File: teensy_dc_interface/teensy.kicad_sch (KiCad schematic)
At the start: 1 part, among them U2 Teensy4.0

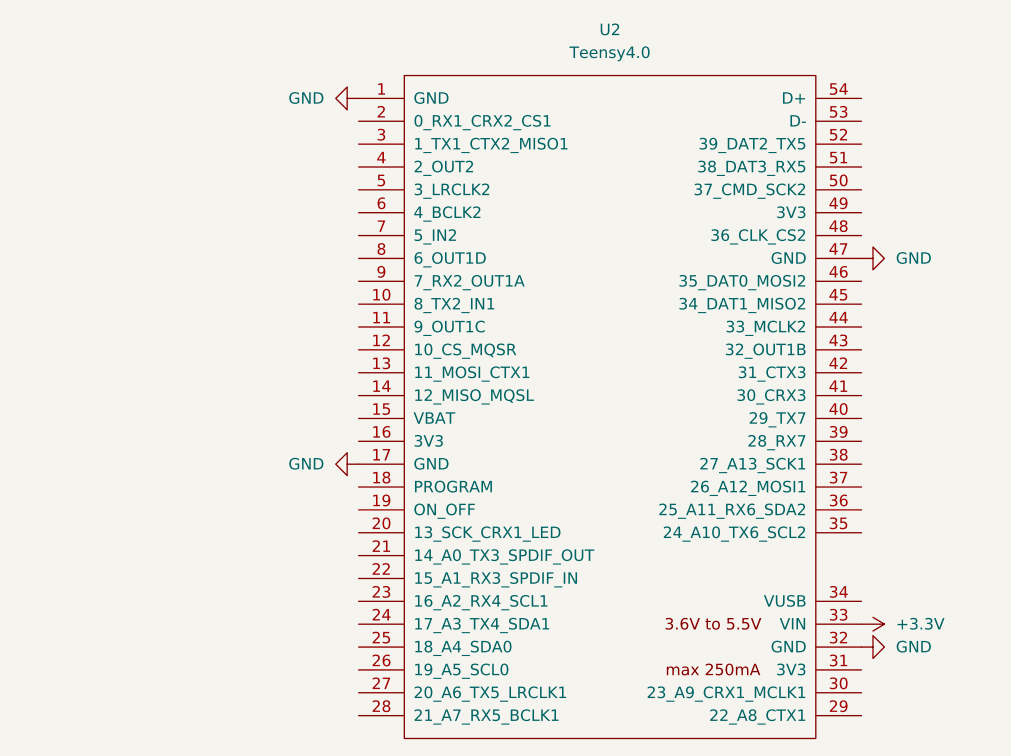
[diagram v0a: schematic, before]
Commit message: teensy to dac connections
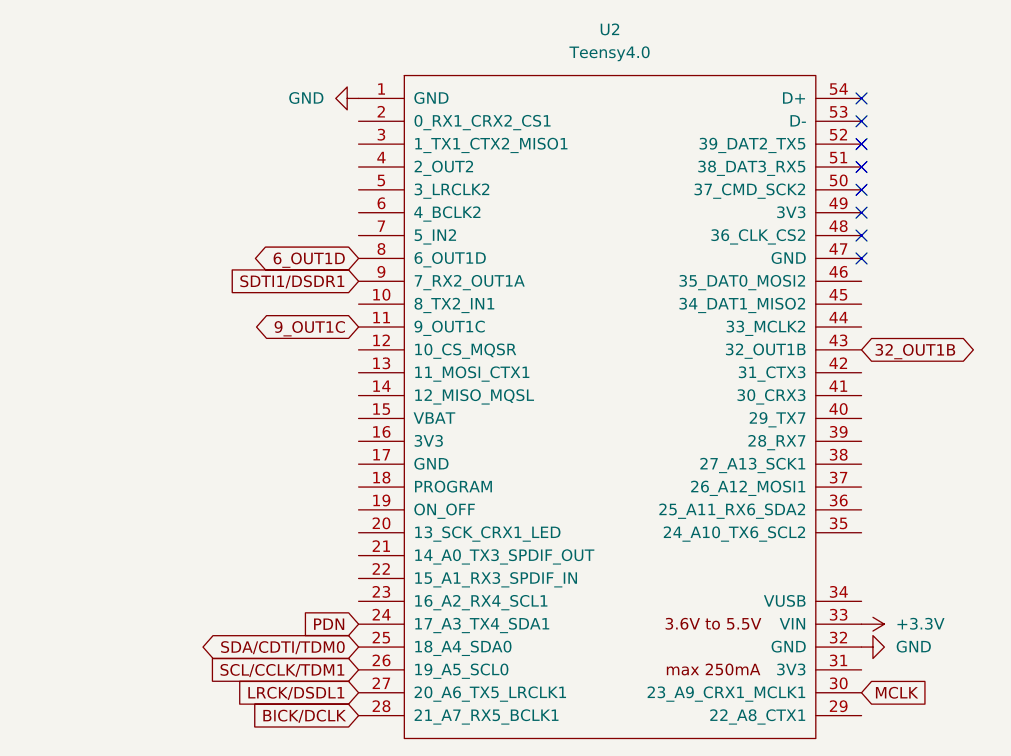
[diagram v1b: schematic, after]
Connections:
- net GND: no longer U2.17 (GND), U2.47 (GND)
- net 9_OUT1C: now reaches U2.11 (9_OUT1C)
- net PDN: now reaches U2.24 (17_A3_TX4_SDA1)
- net SDA/CDTI/TDM0: now reaches U2.25 (18_A4_SDA0)
- net SCL/CCLK/TDM1: now reaches U2.26 (19_A5_SCL0)
- net LRCK/DSDL1: now reaches U2.27 (20_A6_TX5_LRCLK1)
- net BICK/DCLK: now reaches U2.28 (21_A7_RX5_BCLK1)
- net MCLK: now reaches U2.30 (23_A9_CRX1_MCLK1)
- net 32_OUT1B: now reaches U2.43 (32_OUT1B)
- net 6_OUT1D: now reaches U2.8 (6_OUT1D)
- net SDTI1/DSDR1: now reaches U2.9 (7_RX2_OUT1A)
- no-connect marks 0 -> 8
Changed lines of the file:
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@@
 	(generator_version "8.0")
 	(paper "A4")
+	(no_connect
+		(at 110.49 53.34)
+	)
+	(no_connect
+		(at 110.49 58.42)
+	)
+	(no_connect
+		(at 110.49 50.8)
+	)
+	(no_connect
+		(at 110.49 66.04)
+	)
+	(no_connect
+		(at 110.49 55.88)
+	)
+	(no_connect
+		(at 110.49 60.96)
+	)
+	(no_connect
+		(at 110.49 68.58)
+	)
+	(no_connect
+		(at 110.49 63.5)
+	)
+	(global_label "6_OUT1D"
+		(shape bidirectional)
+		(at 54.61 68.58 180)
+		(effects
+			(font
+				(size 1.27 1.27)
+			)
+			(justify right)
+		)
+		(property "Intersheetrefs" "${INTERSHEET_REFS}"
+			(at 54.61 68.58 0)
+			(effects
+				(font
+					(size 1.27 1.27)
+				)
+				(hide yes)
+			)
+		)
+	)
+	(global_label "SDTI1/DSDR1"
+		(shape input)
+		(at 54.61 71.12 180)
+		(effects
+			(font
+				(size 1.27 1.27)
+			)
+			(justify right)
+		)
+		(property "Intersheetrefs" "${INTERSHEET_REFS}"
+			(at 54.61 71.12 0)
+			(effects
+				(font
+					(size 1.27 1.27)
+				)
+				(hide yes)
+			)
+		)
+	)
+	(global_label "SDA/CDTI/TDM0"
+		(shape bidirectional)
+		(at 54.61 111.76 180)
+		(effects
+			(font
+				(size 1.27 1.27)
+			)
+			(justify right)
+		)
+		(property "Intersheetrefs" "${INTERSHEET_REFS}"
+			(at 54.61 111.76 0)
+			(effects
+				(font
+					(size 1.27 1.27)
+				)
+				(hide yes)
+			)
+		)
+	)
+	(global_label "32_OUT1B"
+		(shape bidirectional)
+		(at 110.49 78.74 0)
+		(effects
+			(font
+				(size 1.27 1.27)
+			)
+			(justify left)
+		)
+		(property "Intersheetrefs" "${INTERSHEET_REFS}"
+			(at 110.49 78.74 0)
+			(effects
+				(font
+					(size 1.27 1.27)
+				)
+				(hide yes)
+			)
+		)
+	)
+	(global_label "MCLK"
+		(shape input)
+		(at 110.49 116.84 0)
+		(effects
+			(font
+				(size 1.27 1.27)
+			)
+			(justify left)
+		)
+		(property "Intersheetrefs" "${INTERSHEET_REFS}"
+			(at 110.49 116.84 0)
+			(effects
+				(font
+					(size 1.27 1.27)
+				)
+				(hide yes)
+			)
+		)
+	)
+	(global_label "9_OUT1C"
+		(shape bidirectional)
+		(at 54.61 76.2 180)
+		(effects
+			(font
+				(size 1.27 1.27)
+			)
+			(justify right)
+		)
+		(property "Intersheetrefs" "${INTERSHEET_REFS}"
+			(at 54.61 76.2 0)
+			(effects
+				(font
+					(size 1.27 1.27)
+				)
+				(hide yes)
+			)
+		)
+	)
+	(global_label "BICK/DCLK"
+		(shape input)
+		(at 54.61 119.38 180)
+		(effects
+			(font
+				(size 1.27 1.27)
+			)
+			(justify right)
+		)
+		(property "Intersheetrefs" "${INTERSHEET_REFS}"
+			(at 54.61 119.38 0)
+			(effects
+				(font
+					(size 1.27 1.27)
+				)
+				(hide yes)
+			)
+		)
+	)
+	(global_label "SCL/CCLK/TDM1"
+		(shape input)
+		(at 54.61 114.3 180)
+		(effects
+			(font
+				(size 1.27 1.27)
+			)
+			(justify right)
+		)
+		(property "Intersheetrefs" "${INTERSHEET_REFS}"
+			(at 54.61 114.3 0)
+			(effects
+				(font
+					(size 1.27 1.27)
+				)
+				(hide yes)
+			)
+		)
+	)
+	(global_label "LRCK/DSDL1"
+		(shape input)
+		(at 54.61 116.84 180)
+		(effects
+			(font
+				(size 1.27 1.27)
+			)
+			(justify right)
+		)
+		(property "Intersheetrefs" "${INTERSHEET_REFS}"
+			(at 54.61 116.84 0)
+			(effects
+				(font
+					(size 1.27 1.27)
+				)
+				(hide yes)
+			)
+		)
+	)
+	(global_label "PDN"
+		(shape input)
+		(at 54.61 109.22 180)
+		(effects
+			(font
+				(size 1.27 1.27)
+			)
+			(justify right)
+		)
+		(property "Intersheetrefs" "${INTERSHEET_REFS}"
+			(at 54.61 109.22 0)
+			(effects
+				(font
+					(size 1.27 1.27)
+				)
+				(hide yes)
+			)
+		)
+	)
 	(symbol
 		(lib_id "4ms_Power-symbol:+3.3V")
@@
 					(unit 1)
 				)
-			)
-		)
-	)
-	(symbol
-		(lib_id "4ms_Power-symbol:GND")
-		(at 110.49 68.58 90)
-		(unit 1)
-		(exclude_from_sim no)
-		(in_bom yes)
-		(on_board yes)
-		(dnp no)
-		(fields_autoplaced yes)
-		(property "Reference" "#PWR038"
-			(at 116.84 68.58 0)
-			(effects
-				(font
-					(size 1.27 1.27)
-				)
-				(hide yes)
-			)
-		)
-		(property "Value" "GND"
-			(at 114.3 68.5799 90)
-			(effects
-				(font
-					(size 1.27 1.27)
-				)
-				(justify right)
-			)
-		)
-		(property "Footprint" ""
-			(at 110.49 68.58 0)
-			(effects
-				(font
-					(size 1.27 1.27)
-				)
-				(hide yes)
-			)
-		)
-		(property "Datasheet" ""
-			(at 110.49 68.58 0)
-			(effects
-				(font
-					(size 1.27 1.27)
-				)
-				(hide yes)
-			)
-		)
-		(property "Description" ""
-			(at 110.49 68.58 0)
-			(effects
-				(font
-					(size 1.27 1.27)
-				)
-				(hide yes)
-			)
-		)
-		(pin "1"
-		)
-		(instances
-			(project "teensy_dc_interface"
-				(path "/a4119639-42c9-4d05-afde-5b738907ed5a/cc1bffa6-65b3-47b9-9487-c9fe2212650d"
-					(reference "#PWR038")
-					(unit 1)
-				)
-			)
-		)
-	)
-	(symbol
-		(lib_id "4ms_Power-symbol:GND")
-		(at 54.61 91.44 270)
-		(unit 1)
-		(exclude_from_sim no)
-		(in_bom yes)
-		(on_board yes)
-		(dnp no)
-		(property "Reference" "#PWR037"
-			(at 48.26 91.44 0)
-			(effects
-				(font
-					(size 1.27 1.27)
-				)
-				(hide yes)
-			)
-		)
-		(property "Value" "GND"
-			(at 50.8 91.4399 90)
-			(effects
-				(font
-					(size 1.27 1.27)
-				)
-				(justify right)
-			)
-		)
-		(property "Footprint" ""
-			(at 54.61 91.44 0)
-			(effects
-				(font
-					(size 1.27 1.27)
-				)
-				(hide yes)
-			)
-		)
-		(property "Datasheet" ""
-			(at 54.61 91.44 0)
-			(effects
-				(font
-					(size 1.27 1.27)
-				)
-				(hide yes)
-			)
-		)
-		(property "Description" ""
-			(at 54.61 91.44 0)
-			(effects
-				(font
-					(size 1.27 1.27)
-				)
-				(hide yes)
-			)
-		)
-		(pin "1"
-		)
-		(instances
-			(project "teensy_dc_interface"
-				(path "/a4119639-42c9-4d05-afde-5b738907ed5a/cc1bffa6-65b3-47b9-9487-c9fe2212650d"
-					(reference "#PWR037")
-					(unit 1)
-				)

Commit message: Updated filtering between VREF's. Added separate power supply for Teensy on 5V. Added test points. Added ADC input
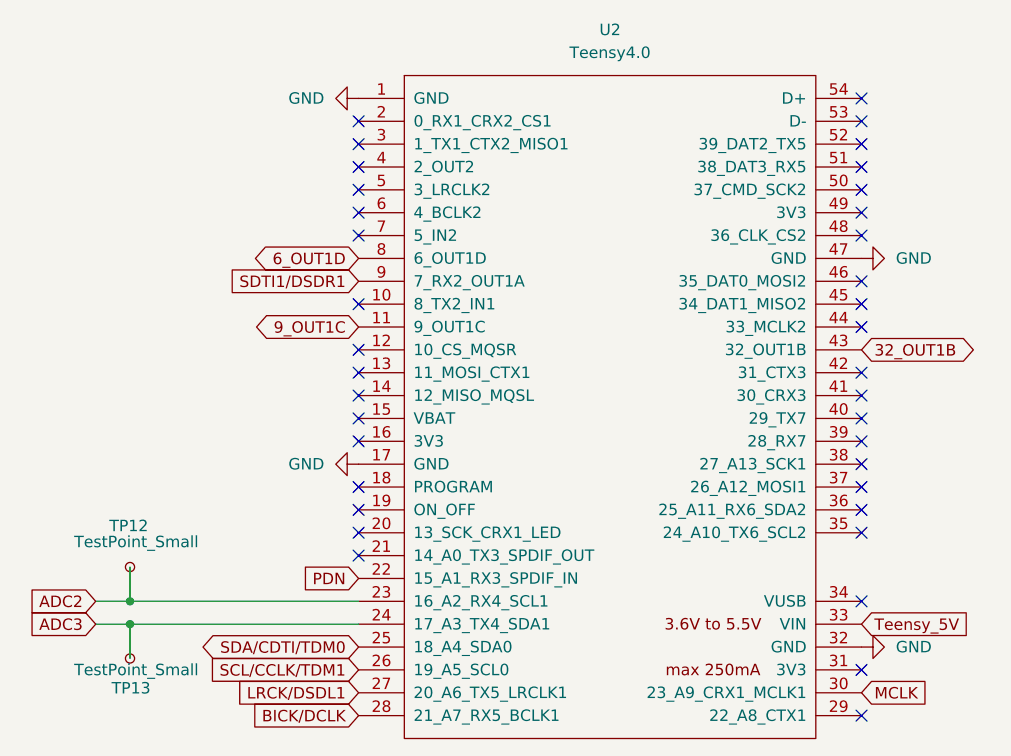
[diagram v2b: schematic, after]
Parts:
- added TP12, TP13: TestPoint_Small, TestPoint:TestPoint_Keystone_5005-5009_Compact, symbol 4ms_Connector:TestPoint_Small
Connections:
- net GND: now also U2.17 (GND), U2.47 (GND)
- net PDN: now also U2.22 (15_A1_RX3_SPDIF_IN); no longer U2.24 (17_A3_TX4_SDA1)
- net ADC2: now reaches U2.23 (16_A2_RX4_SCL1)
- net ADC2: now also TP12.1
- net +3.3V renamed Teensy_5V
- new net ADC3: TP13.1, U2.24 (17_A3_TX4_SDA1)
- no-connect marks 8 -> 37

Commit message: Created first set of DAC outputs layout
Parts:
- U2: footprint teensy:Teensy40 -> teensy:Teensy40_SMT
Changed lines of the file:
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@@
 			)
 		)
-		(property "Footprint" "teensy:Teensy40"
+		(property "Footprint" "teensy:Teensy40_SMT"
 			(at 72.39 80.01 0)
 			(effects

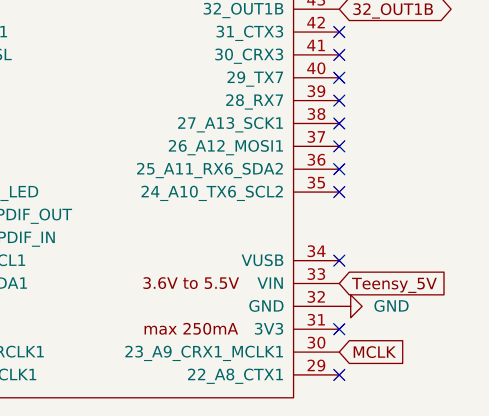
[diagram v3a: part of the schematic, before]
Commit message: out pairs as pages
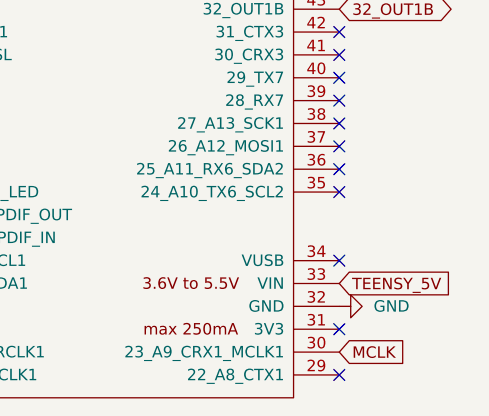
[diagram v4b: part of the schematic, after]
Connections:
- net Teensy_5V renamed TEENSY_5V
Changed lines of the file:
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@@
 		)
 	)
-	(global_label "Teensy_5V"
+	(global_label "TEENSY_5V"
 		(shape input)
 		(at 110.49 109.22 0)
@@
 		)
 		(property "Intersheetrefs" "${INTERSHEET_REFS}"
-			(at 123.0304 109.22 0)
+			(at 123.6351 109.22 0)
 			(effects
 				(font
